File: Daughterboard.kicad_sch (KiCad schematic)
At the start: 131 parts, among them J6 Conn_01x10_MountingPin, SW10 SW_Push, SW11 SW_Push, SW12 SW_Push, SW13 SW_Push, SW14 SW_Push, SW15 SW_Push, SW16 SW_Push, SW17 SW_Push, SW18 SW_Push, SW19 SW_Push, SW3 SW_Push, SW4 SW_Push, SW5 SW_Push, SW6 SW_Push, SW7 SW_Push, SW8 SW_Push, SW9 SW_Push, U4 TSOP34S40F, U5 XPT2046TS, U6 PCM5102A, U7 PAM8403D, U8 PAM8403D

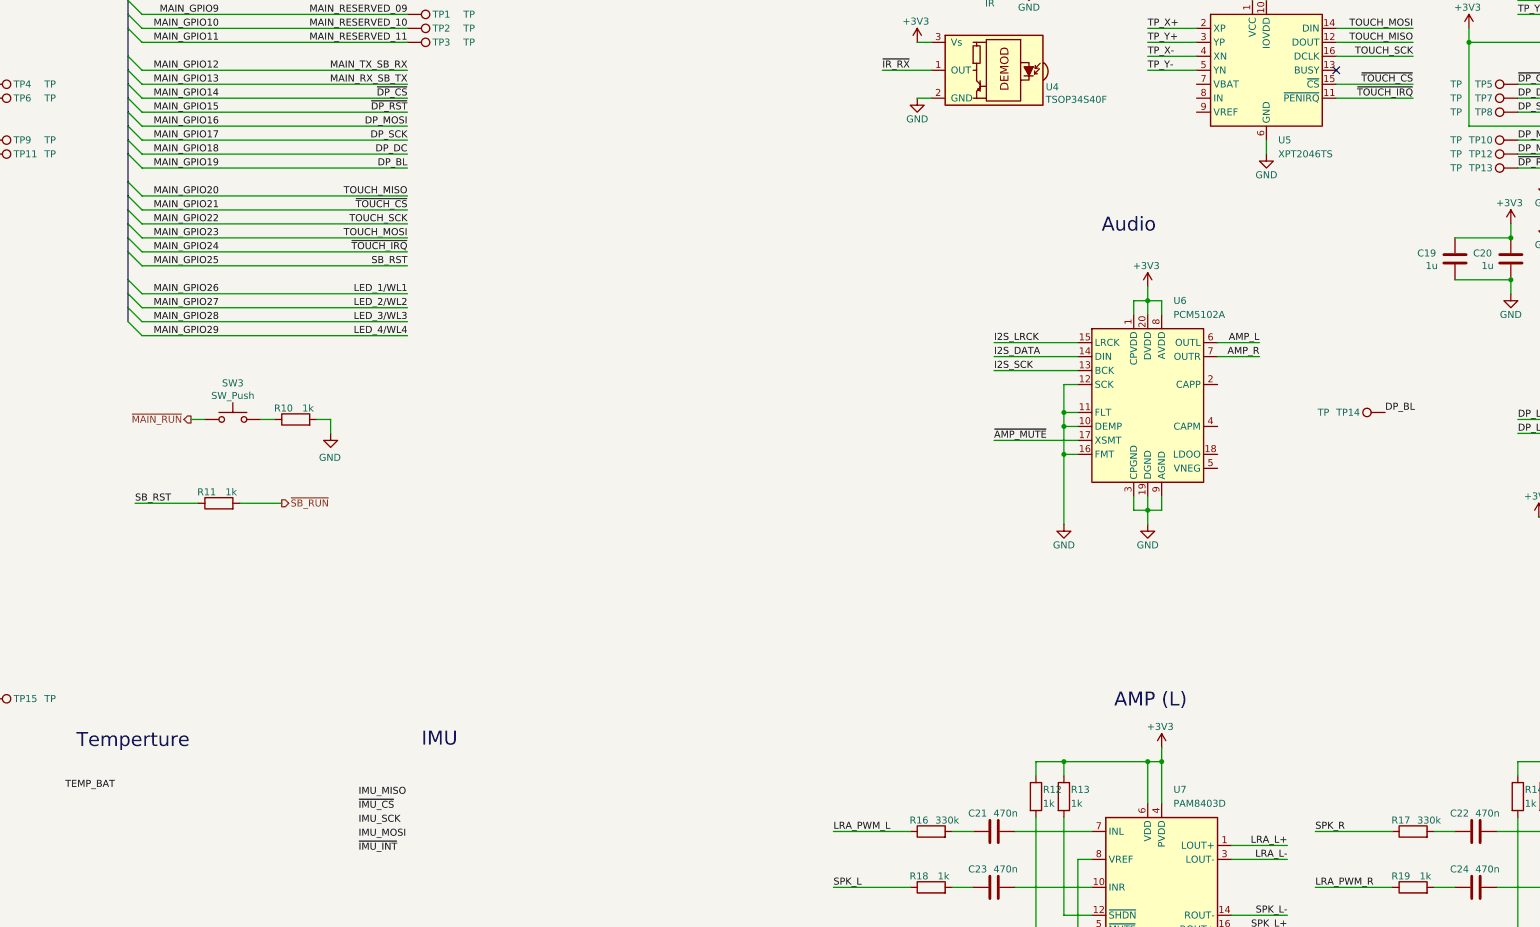
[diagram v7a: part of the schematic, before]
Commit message: Update LCD pin assignments
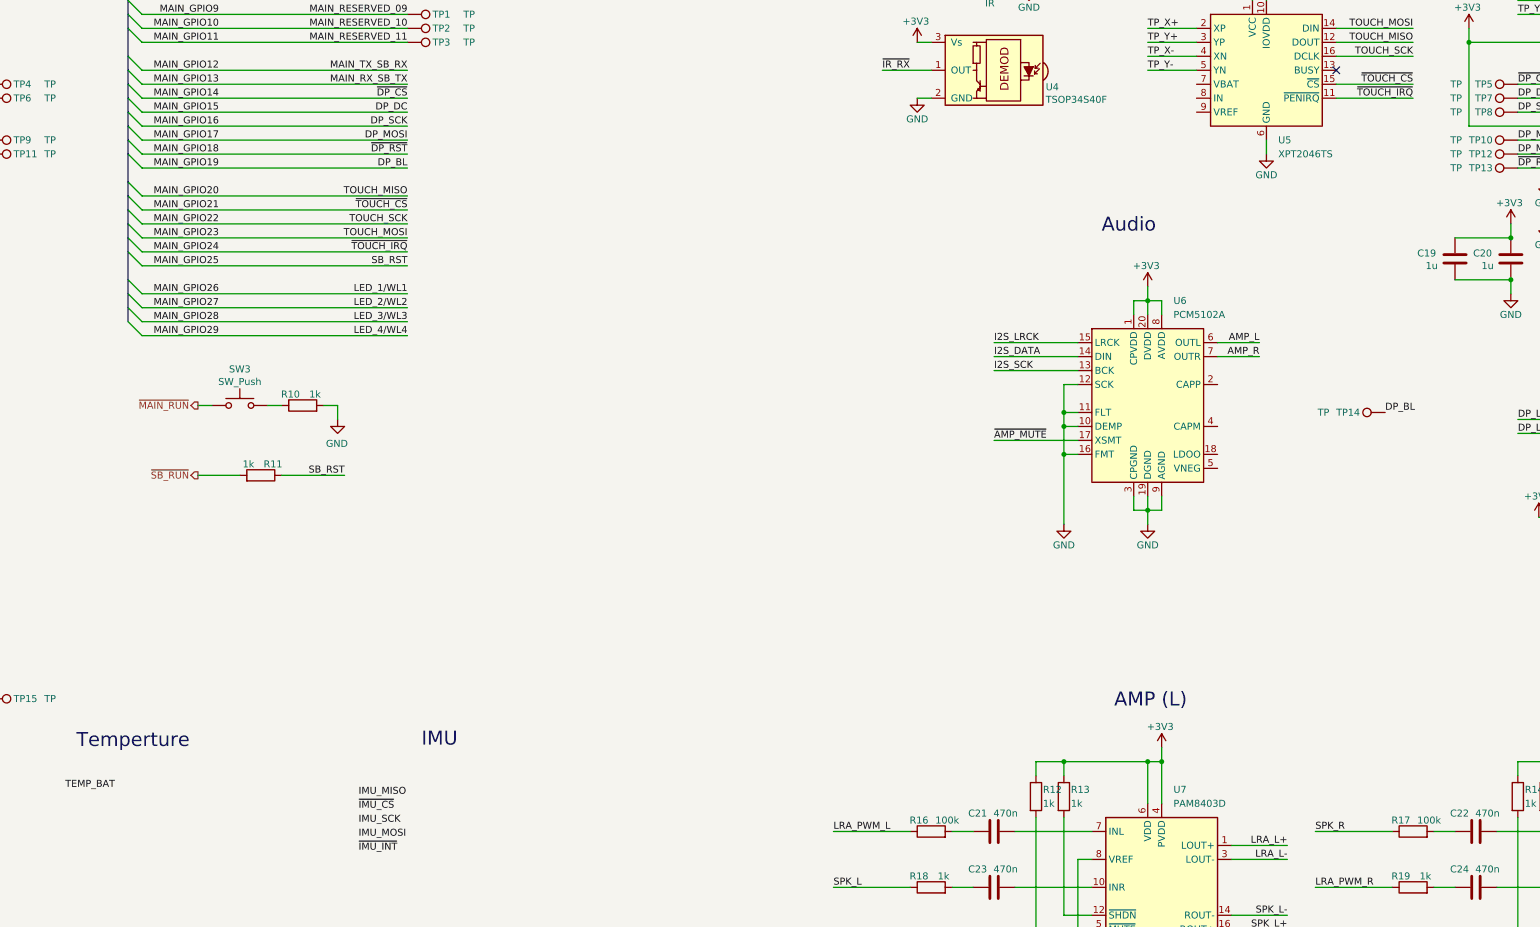
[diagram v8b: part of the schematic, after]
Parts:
- R16, R17: value 330k -> 100k
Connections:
- net MAIN_GPIO15 renamed MAIN_GPIO18
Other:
- moved on the sheet: R10, R11, SW3
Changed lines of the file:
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@@
 	(wire
 		(pts
-			(xy 102.87 121.92) (xy 114.3 121.92)
+			(xy 140.97 116.84) (xy 129.54 116.84)
 		)
 		(stroke
@@
 	(wire
 		(pts
-			(xy 125.73 106.68) (xy 128.27 106.68)
+			(xy 127 104.14) (xy 129.54 104.14)
 		)
 		(stroke
@@
 	(wire
 		(pts
-			(xy 138.43 106.68) (xy 138.43 109.22)
+			(xy 139.7 104.14) (xy 139.7 106.68)
 		)
 		(stroke
@@
 	(wire
 		(pts
-			(xy 135.89 106.68) (xy 138.43 106.68)
+			(xy 137.16 104.14) (xy 139.7 104.14)
 		)
 		(stroke
@@
 	(wire
 		(pts
-			(xy 113.03 106.68) (xy 115.57 106.68)
+			(xy 114.3 104.14) (xy 116.84 104.14)
 		)
 		(stroke
@@
 	(wire
 		(pts
-			(xy 129.54 121.92) (xy 121.92 121.92)
+			(xy 114.3 116.84) (xy 121.92 116.84)
 		)
 		(stroke
@@
 		)
 	)
+	(label "DP_MOSI"
+		(at 152.4 55.88 180)
+		(effects
+			(font
+				(size 1.27 1.27)
+			)
+			(justify right bottom)
+		)
+	)
 	(label "GPIO45"
 		(at 43.18 152.4 180)
@@
 		)
 	)
+	(label "DP_BL"
+		(at 152.4 60.96 180)
+		(effects
+			(font
+				(size 1.27 1.27)
+			)
+			(justify right bottom)
+		)
+	)
 	(label "SB_RST"
 		(at 152.4 78.74 180)
@@
 		)
 	)
-	(label "~{DP_RST}"
-		(at 152.4 50.8 180)
-		(effects
-			(font
-				(size 1.27 1.27)
-			)
-			(justify right bottom)
-		)
-	)
 	(label "LED_4{slash}WL4"
 		(at 152.4 91.44 180)
@@
 		)
 	)
-	(label "~{DP_CS}"
-		(at 152.4 48.26 180)
-		(effects
-			(font
-				(size 1.27 1.27)
-			)
-			(justify right bottom)
-		)
-	)
 	(label "SB_RESERVED_47"
 		(at 76.2 157.48 180)
@@
 		)
 	)
+	(label "~{DP_RST}"
+		(at 152.4 58.42 180)
+		(effects
+			(font
+				(size 1.27 1.27)
+			)
+			(justify right bottom)
+		)
+	)
 	(label "~{IMU_INT}"
 		(at 76.2 96.52 180)
@@
 		)
 	)
-	(label "DP_DC"
-		(at 152.4 58.42 180)
-		(effects
-			(font
-				(size 1.27 1.27)
-			)
-			(justify right bottom)
-		)
-	)
 	(label "LED_2"
 		(at 46.99 243.84 0)
@@
 	)
 	(label "SB_RST"
-		(at 102.87 121.92 0)
+		(at 140.97 116.84 180)
 		(effects
 			(font
 				(size 1.27 1.27)
 			)
-			(justify left bottom)
+			(justify right bottom)
 		)
 	)
@@
 		)
 	)
-	(label "DP_MOSI"
-		(at 152.4 53.34 180)
+	(label "DP_DC"
+		(at 152.4 50.8 180)
 		(effects
 			(font
@@
 		)
 	)
+	(label "DP_SCK"
+		(at 152.4 53.34 180)
+		(effects
+			(font
+				(size 1.27 1.27)
+			)
+			(justify right bottom)
+		)
+	)
 	(label "HSTX_2"
 		(at 76.2 68.58 180)
@@
 		)
 	)
+	(label "~{DP_CS}"
+		(at 152.4 48.26 180)
+		(effects
+			(font
+				(size 1.27 1.27)
+			)
+			(justify right bottom)
+		)
+	)
 	(label "BTN_H1"
 		(at 76.2 116.84 180)
@@
 		)
 	)
-	(label "DP_BL"
-		(at 152.4 60.96 180)
-		(effects
-			(font
-				(size 1.27 1.27)
-			)
-			(justify right bottom)
-		)
-	)
 	(label "TOUCH_MISO"
 		(at 152.4 66.04 180)
@@
 		)
 	)
-	(label "DP_SCK"
-		(at 152.4 55.88 180)
-		(effects
-			(font
-				(size 1.27 1.27)
-			)
-			(justify right bottom)
-		)
-	)
 	(label "Joy2_X"
 		(at 91.44 262.89 0)
@@
 	(hierarchical_label "~{SB_RUN}"
 		(shape output)
-		(at 129.54 121.92 0)
+		(at 114.3 116.84 180)
 		(effects
 			(font
 				(size 1.27 1.27)
 			)
-			(justify left)
+			(justify right)
 		)
 	)
 	(hierarchical_label "~{MAIN_RUN}"
 		(shape output)
-		(at 113.03 106.68 180)
+		(at 114.3 104.14 180)
 		(effects
 			(font
@@
 			)
 		)
-		(property "Value" "330k"
+		(property "Value" "100k"
 			(at 252.73 179.578 90)
 			(effects
@@
 	(symbol
 		(lib_id "power:GND")
-		(at 138.43 109.22 0)
+		(at 139.7 106.68 0)
 		(mirror y)
 		(unit 1)
@@
 		(dnp no)
 		(property "Reference" "#PWR046"
-			(at 138.43 115.57 0)
+			(at 139.7 113.03 0)
 			(effects
 				(font
@@
 		)
 		(property "Value" "GND"
-			(at 138.303 113.6142 0)
+			(at 139.573 111.0742 0)
 			(effects
 				(font
@@
 		)
 		(property "Footprint" ""
-			(at 138.43 109.22 0)
+			(at 139.7 106.68 0)
 			(effects
 				(font
@@
 		)
 		(property "Datasheet" ""
-			(at 138.43 109.22 0)
+			(at 139.7 106.68 0)
 			(effects
 				(font
@@
 		)
 		(property "Description" ""
-			(at 138.43 109.22 0)
+			(at 139.7 106.68 0)
 			(effects
 				(font
@@
 	(symbol
 		(lib_id "Device:R")
-		(at 118.11 121.92 90)
+		(at 125.73 116.84 270)
+		(mirror x)
 		(unit 1)
 		(exclude_from_sim no)
@@
 		(dnp no)
 		(property "Reference" "R11"
-			(at 117.602 119.888 90)
+			(at 126.238 114.808 90)
 			(effects
 				(font
@@
 		)
 		(property "Value" "1k"
-			(at 121.412 119.888 90)
+			(at 122.428 114.808 90)
 			(effects
 				(font
@@
 		)
 		(property "Footprint" "Resistor_SMD:R_0402_1005Metric_Pad0.72x0.64mm_HandSolder"
-			(at 118.11 123.698 90)
+			(at 125.73 118.618 90)
 			(effects
 				(font
@@
 		)
 		(property "Datasheet" "~"
-			(at 118.11 121.92 0)
+			(at 125.73 116.84 0)
 			(effects
 				(font
@@
 		)
 		(property "Description" "Resistor"
-			(at 118.11 121.92 0)
+			(at 125.73 116.84 0)
 			(effects
 				(font
@@
 	(symbol
 		(lib_id "Switch:SW_Push")
-		(at 120.65 106.68 0)
+		(at 121.92 104.14 0)
 		(unit 1)
 		(exclude_from_sim no)
@@
 		(dnp no)
 		(property "Reference" "SW3"
-			(at 120.65 100.076 0)
+			(at 121.92 97.536 0)
 			(effects
 				(font
@@
 		)
 		(property "Value" "SW_Push"
-			(at 120.65 102.362 0)
+			(at 121.92 99.822 0)
 			(effects
 				(font
@@
 		)
 		(property "Footprint" "Button_Switch_SMD:SW_Push_1P1T_NO_Vertical_Wuerth_434133025816"
-			(at 120.65 101.6 0)
+			(at 121.92 99.06 0)
 			(effects
 				(font
@@
 		)
 		(property "Datasheet" "~"
-			(at 120.65 101.6 0)
+			(at 121.92 99.06 0)
 			(effects
 				(font
@@
 		)
 		(property "Description" "Push button switch, generic, two pins"
-			(at 120.65 106.68 0)
+			(at 121.92 104.14 0)
 			(effects
 				(font
@@
 	(symbol
 		(lib_id "Device:R")
-		(at 132.08 106.68 90)
+		(at 133.35 104.14 90)
 		(unit 1)
 		(exclude_from_sim no)
@@
 		(dnp no)
 		(property "Reference" "R10"
-			(at 131.572 104.648 90)
+			(at 132.842 102.108 90)
 			(effects
 				(font
@@
 		)
 		(property "Value" "1k"
-			(at 135.382 104.648 90)
+			(at 136.652 102.108 90)
 			(effects
 				(font
@@
 		)
 		(property "Footprint" "Resistor_SMD:R_0402_1005Metric_Pad0.72x0.64mm_HandSolder"
-			(at 132.08 108.458 90)
+			(at 133.35 105.918 90)
 			(effects
 				(font
@@
 		)
 		(property "Datasheet" "~"
-			(at 132.08 106.68 0)
+			(at 133.35 104.14 0)
 			(effects
 				(font
@@
 		)
 		(property "Description" "Resistor"
-			(at 132.08 106.68 0)
+			(at 133.35 104.14 0)
 			(effects
 				(font
@@
 			)
 		)
-		(property "Value" "330k"
+		(property "Value" "100k"
 			(at 340.36 179.578 90)
 			(effects
